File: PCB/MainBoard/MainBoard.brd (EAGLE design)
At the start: 60 x 75 mm, 94 parts, among them IC1 LD1085D2T33R, Q2 CSM-7X-DU, U1 LM1084IS-5.0/NOPB, U4 STM32H753VIT6, U5 LM1084IS-5.0/NOPB

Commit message: Update eagle files
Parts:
- removed C1, C4: 100nF, rcl:C0805
- removed C2, C3: 100uF, rcl:C0805
- removed U1: LM1084IS-5.0/NOPB, LM1084IS-5.0_NOPB:TO254P1524X483-4N
- moved ON/OFF 125.1 mm to (30.0, 22.0), turned to 180 degrees
- moved IC1 104.5 mm to (46.0, 36.0), flipped to the bottom, turned to 180 degrees
- moved C5 101.7 mm to (24.0, 37.0), flipped to the bottom, turned to 90 degrees
- moved PRAWY_TYL 92.7 mm to (14.0, 59.5)
- moved C32 92.0 mm to (128.6, 20.8)
- moved C21 92.0 mm to (117.5, 49.7)
- moved C43 91.0 mm to (115.3, 21.0)
- moved C33 91.0 mm to (116.6, 54.0)
- moved C19 91.0 mm to (133.3, 44.2)
- moved C22 91.0 mm to (111.7, 45.4)
- moved C23 91.0 mm to (111.6, 39.5)
- moved C35 91.0 mm to (135.7, 44.3)
- moved C36 91.0 mm to (109.0, 45.6)
- moved C40 91.0 mm to (127.8, 27.1)
- moved C41 91.0 mm to (115.7, 27.2)
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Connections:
- new net N$88: C24.2, C27.2, U5.1
- net +5V: now also C5.1, C6.1, IC1.3, U5.2, U5.4; no longer C3.1, C4.1, U1.2, U1.4
- net GND: no longer C1.2, C2.2, C24.2, C27.2, C3.2, C4.2, U1.1, U5.1
- net V_BAT: no longer C1.1, C2.1, C5.1, C6.1, IC1.3, U1.3, U5.2, U5.4
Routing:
- net +5V: track 0.00 -> 27.3 mm
- net V_BAT: track 0.00 -> 18.9 mm
- net +3V3: track 0.00 -> 5.57 mm
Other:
- outline, holes or cut-outs redrawn

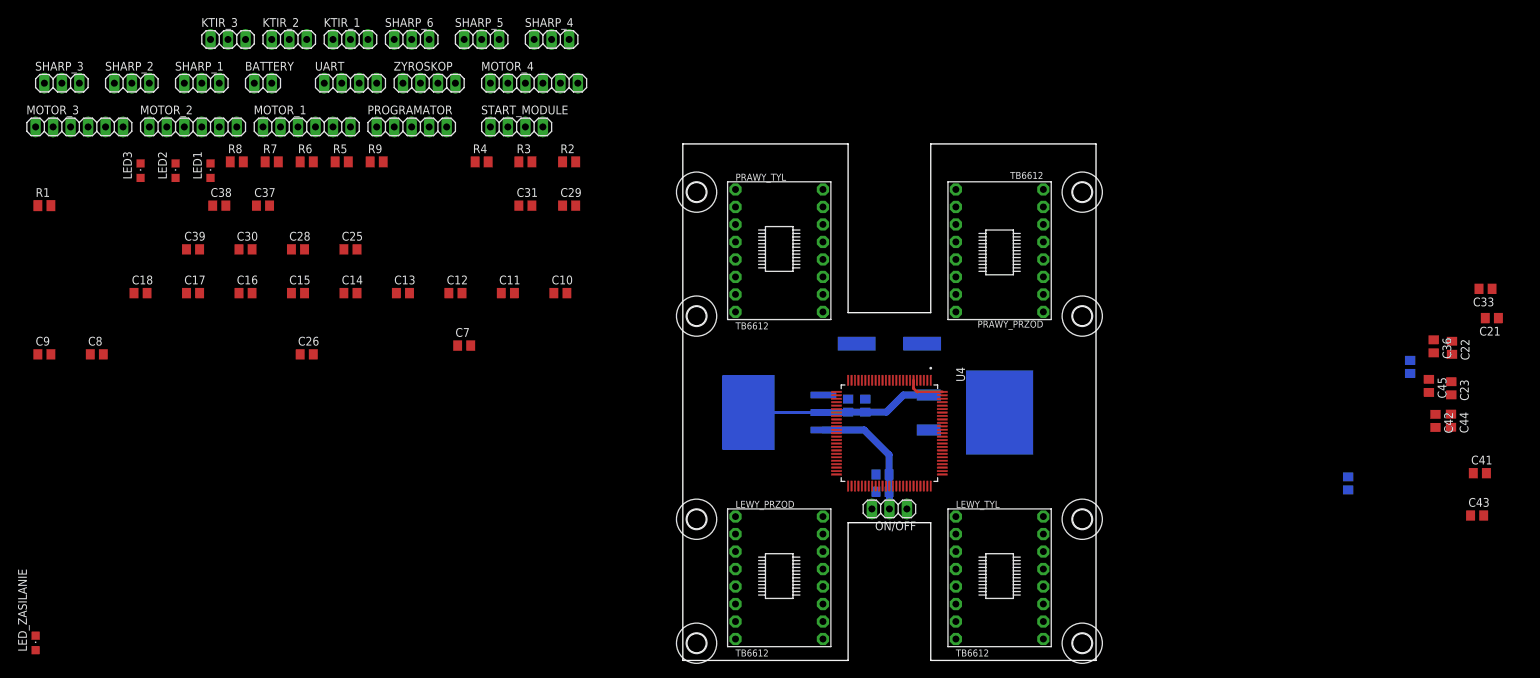
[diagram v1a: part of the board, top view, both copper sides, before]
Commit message: PCB update
-place elements on the board
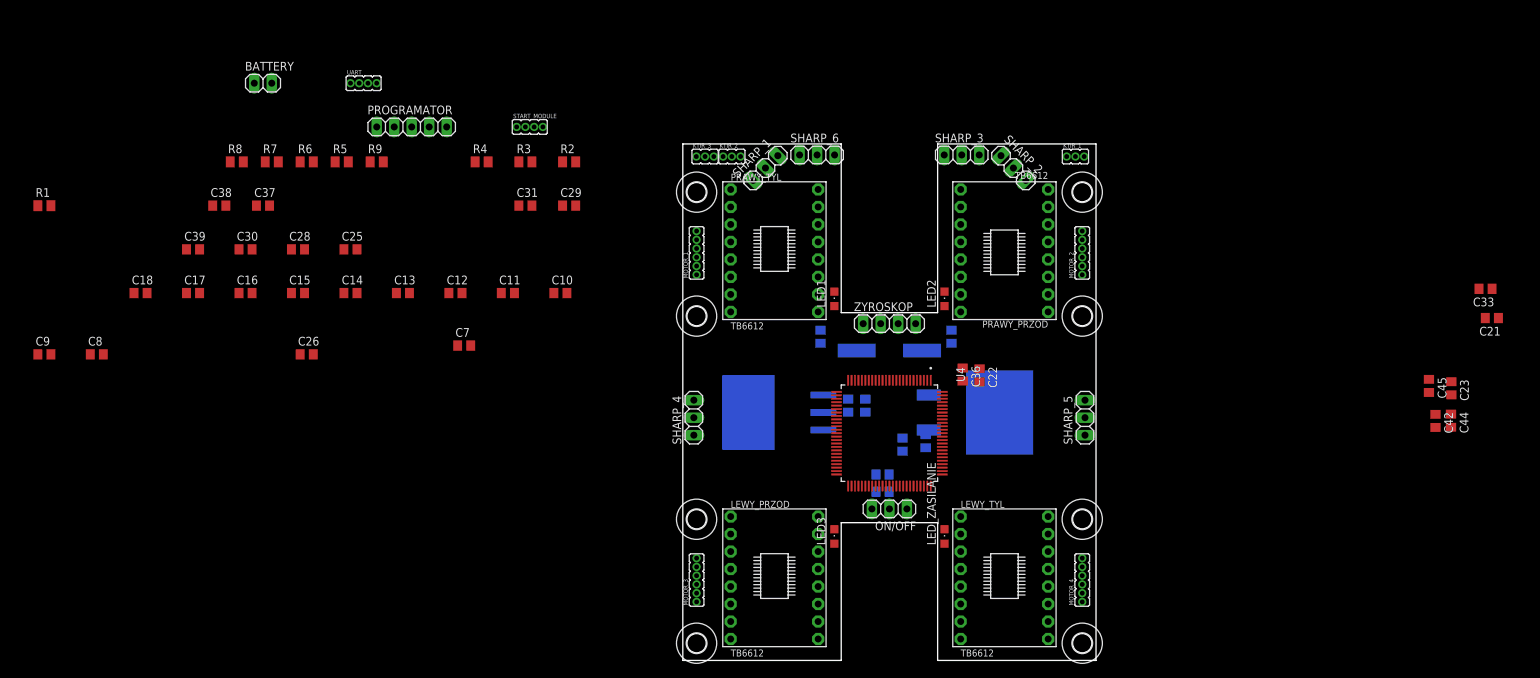
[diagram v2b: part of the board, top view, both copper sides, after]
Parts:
- KTIR_1, KTIR_2, KTIR_3: value (none) -> PH1X3-05; device pinhead:1X03 -> pinhrad:PH005-1-3
- MOTOR_1, MOTOR_2, MOTOR_3, MOTOR_4: value (none) -> PH1X6-05; device pinhead:1X06 -> pinhrad:PH005-1-6
- START_MODULE, UART: value (none) -> PH1X4-05; device pinhead:1X04 -> pinhrad:PH005-1-4
- moved LED_ZASILANIE 132.9 mm to (38.0, 18.0)
- moved SHARP_3 131.1 mm to (40.5, 73.4)
- moved MOTOR_2 130.9 mm to (58.0, 56.0), turned to 90 degrees
- moved SHARP_2 128.6 mm to (48.0, 71.5), turned to 315 degrees
- moved LED3 113.9 mm to (22.0, 18.0)
- moved LED2 113.2 mm to (38.0, 52.5)
- moved MOTOR_3 113.1 mm to (2.00, 8.50), turned to 90 degrees
- moved MOTOR_4 109.6 mm to (58.0, 8.50), turned to 90 degrees
- moved KTIR_1 105.4 mm to (55.7, 73.2)
- moved SHARP_5 103.4 mm to (58.4, 35.2), turned to 90 degrees
- moved LED1 92.5 mm to (22.0, 52.5)
- moved C41 83.9 mm to (31.9, 31.3), flipped to the bottom, turned to 270 degrees
- moved SHARP_1 82.8 mm to (12.0, 71.5), turned to 45 degrees
- moved C43 80.8 mm to (35.3, 31.8), flipped to the bottom, turned to 270 degrees
- moved C46 79.5 mm to (20.0, 47.0)
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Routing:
- net +5V: track 27.3 -> 0.00 mm
- net V_BAT: track 18.9 -> 0.00 mm
- net +3V3: track 5.57 -> 0.00 mm
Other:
- outline, holes or cut-outs redrawn

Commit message: Update pcb files
- edit positions on the board
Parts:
- added R13: 100R, rcl:M0805
- added R14, R15: 47R, rcl:M0805
- PROGRAMATOR: value (none) -> FTSH-107-01-F-DV-K; device pinhead:1X05 -> FTSH-107-01-F-DV-K:SAMTEC_FTSH-107-01-F-DV-K
- moved R8 118.8 mm to (38.1, 13.0), turned to 90 degrees
- moved BATTERY 113.5 mm to (34.0, 21.6)
- moved R7 100.9 mm to (21.9, 13.0), turned to 90 degrees
- moved START_MODULE 97.6 mm to (58.5, 25.5), turned to 90 degrees
- moved R6 93.9 mm to (38.1, 57.5), turned to 90 degrees
- moved UART 76.7 mm to (1.50, 25.5), turned to 90 degrees
- moved R5 73.0 mm to (21.9, 57.5), turned to 90 degrees
- moved PROGRAMATOR 65.9 mm to (11.0, 35.0), turned to 90 degrees
- moved ON/OFF 3.03 mm to (27.0, 21.6)
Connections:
- net N$30 renamed JRST
- removed net N$18: U4.60
- removed net N$22: U4.39
- removed net N$24: U4.28
- removed net N$25: U4.29
- removed net N$26: U4.30
- removed net N$27: U4.31
- removed net N$28: U4.77
- removed net N$29: U4.89
- removed net N$31: U4.91
- removed net N$33: U4.22
- removed net N$34: U4.23
- removed net N$38: U4.34
- removed net N$40: U4.93
- removed net N$43: U4.15
- removed net N$63: U4.43
- removed net N$65: U4.41
- removed net N$67: U4.61
- removed net N$74: U4.65
- removed net N$75: U4.64
- removed net N$76: U4.63
- removed net N$86: U4.72
- removed net N$87: U4.76
- removed net SWCLK: PROGRAMATOR.2
- removed net SWDIO: PROGRAMATOR.4
- new net JCLK: R15.1, U4.76
- new net JTDI: PROGRAMATOR.10, U4.77
- new net JTDO: PROGRAMATOR.08, U4.89
- new net JTMS: PROGRAMATOR.04, U4.72
- net +3V3: now also PROGRAMATOR.03; no longer PROGRAMATOR.1
- net BAT_ADC: now also U4.15
- net ENK_LP_A: now also U4.39
- net ENK_LP_B: now also U4.41
- net ENK_LT_B: now also U4.31, U4.91
- net ENK_PP_A: now also U4.59
- net ENK_PP_B: now also U4.60
- net ENK_PT_A: now also U4.63
- net ENK_PT_B: now also U4.64
- net GND: now also PROGRAMATOR.05, PROGRAMATOR.07, R13.2; no longer PROGRAMATOR.3
- net KTIR_1: now also U4.28
- net KTIR_2: now also U4.29
- net KTIR_3: now also U4.30
- net N$1: now also PROGRAMATOR.11, R13.1; no longer C25.2, R2.1, U4.14
- net N$17: now also PROGRAMATOR.06, R15.2; no longer U4.59
- net N$8: now also PROGRAMATOR.12, R14.2; no longer U4.92
- net NRST: now also C25.2, R14.1, R2.1, U4.14; no longer PROGRAMATOR.5
- net PWM_LP: now also U4.43
- net PWM_LT: now also U4.34
- net PWM_PP: now also U4.61
- net PWM_PT: now also U4.65
- net RX: now also U4.22
- net SCL: now also U4.92
- net SDA: now also U4.93
- net TX: now also U4.23

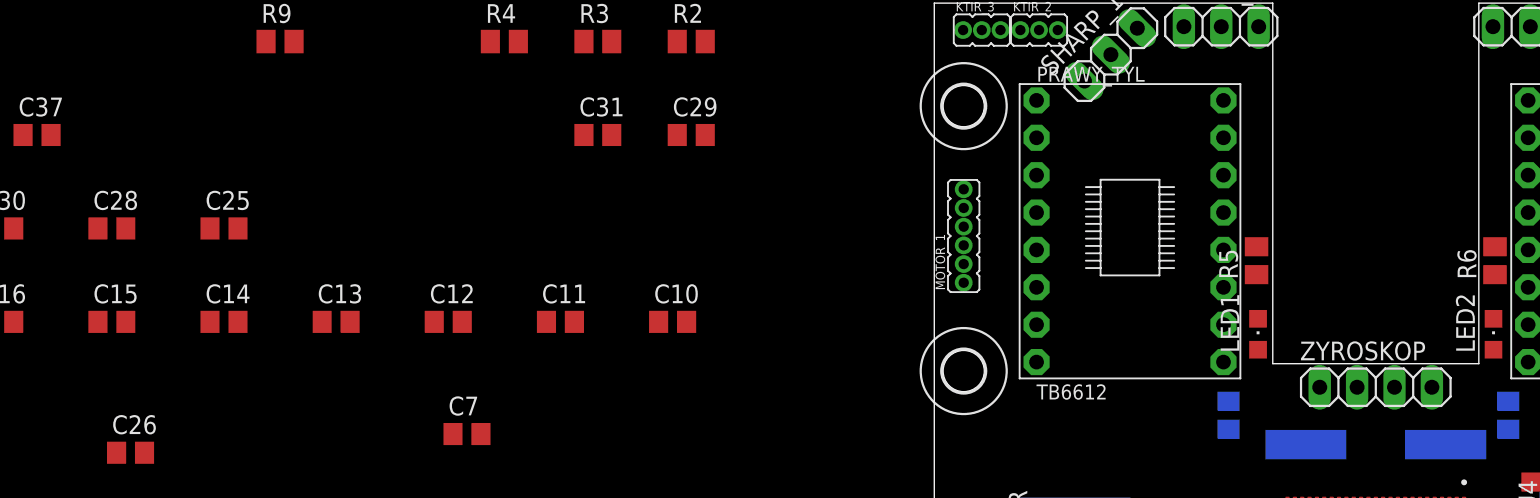
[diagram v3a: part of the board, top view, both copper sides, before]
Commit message: Update eagle files
-delete gyroscope
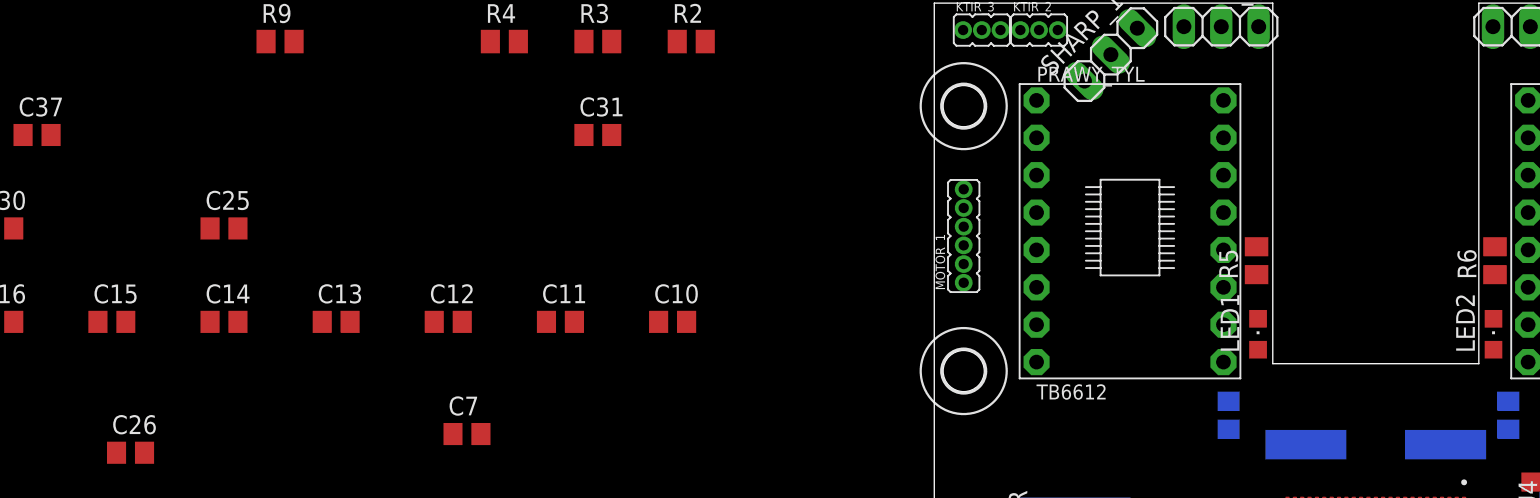
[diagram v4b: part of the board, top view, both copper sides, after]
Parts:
- removed C28: 100nF, rcl:C0805
- removed C29: 10uF, rcl:C0805
- removed ZYROSKOP: (no value), pinhead:1X04
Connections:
- net +3V3: no longer C28.2, C29.2, ZYROSKOP.4
- net GND: no longer C28.1, C29.1, ZYROSKOP.3
- net SCL: no longer ZYROSKOP.1
- net SDA: no longer ZYROSKOP.2
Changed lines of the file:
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@@
 <element name="C26" library="rcl" package="C0805" value="2.2uf(ceramic)" x="-54.61" y="44.45"/>
 <element name="C27" library="rcl" package="C0805" value="100uF" x="29" y="27" rot="MR0"/>
-<element name="C28" library="rcl" package="C0805" value="100nF" x="-55.88" y="59.69"/>
-<element name="C29" library="rcl" package="C0805" value="10uF" x="-16.51" y="66.04"/>
 <element name="C30" library="rcl" package="C0805" value="100nF" x="-63.5" y="59.69"/>
 <element name="C31" library="rcl" package="C0805" value="10uF" x="-22.86" y="66.04"/>
@@
 </element>
 <element name="UART" library="pinhrad" package="PH005-1-4" value="PH1X4-05" x="1.5" y="25.5" rot="R90"/>
-<element name="ZYROSKOP" library="pinhead" package="1X04" value="" x="30" y="48.9"/>
 <element name="U$1" library="holes" package="2,8" value="" x="2" y="2.5"/>
 <element name="U$2" library="holes" package="2,8" value="" x="2" y="20.5"/>
@@
 <contactref element="C37" pad="1"/>
 <contactref element="C18" pad="1"/>
-<contactref element="ZYROSKOP" pad="3"/>
-<contactref element="C29" pad="1"/>
-<contactref element="C28" pad="1"/>
 <contactref element="LED1" pad="C"/>
 <contactref element="LED2" pad="C"/>
@@
 <wire x1="24" y1="37.95" x2="26.5" y2="37.95" width="0" layer="19" extent="16-16"/>
 <wire x1="22.32" y1="39" x2="24" y2="37.95" width="0" layer="19" extent="1-16"/>
-<wire x1="31.27" y1="48.9" x2="39" y2="47.95" width="0" layer="19" extent="16-16"/>
 <wire x1="20" y1="47.95" x2="22.32" y2="39" width="0" layer="19" extent="1-16"/>
 <wire x1="19.65" y1="50.61" x2="20" y2="47.95" width="0" layer="19" extent="16-16"/>
 <wire x1="22" y1="53.55" x2="19.65" y2="50.61" width="0" layer="19" extent="1-1"/>
+<wire x1="13.035" y1="35" x2="22.32" y2="39" width="0" layer="19" extent="1-1"/>
+<wire x1="13.035" y1="33.73" x2="13.035" y2="35" width="0" layer="19" extent="1-1"/>
 <wire x1="22.32" y1="27.5" x2="24" y2="37.95" width="0" layer="19" extent="1-16"/>
 <wire x1="22" y1="19.05" x2="22.32" y2="27.5" width="0" layer="19" extent="1-1"/>
+<wire x1="1.6" y1="35.25" x2="13.035" y2="35" width="0" layer="19" extent="1-1"/>
+<wire x1="1.5" y1="28.04" x2="1.6" y2="35.25" width="0" layer="19" extent="1-1"/>
+<wire x1="6.95" y1="20.89" x2="1.5" y2="28.04" width="0" layer="19" extent="1-1"/>
+<wire x1="2" y1="14.85" x2="6.95" y2="20.89" width="0" layer="19" extent="1-1"/>
 <wire x1="6.95" y1="50.61" x2="19.65" y2="50.61" width="0" layer="19" extent="1-1"/>
 <wire x1="2" y1="62.35" x2="6.95" y2="50.61" width="0" layer="19" extent="1-1"/>
@@
 <wire x1="12" y1="71.5" x2="6.95" y2="68.39" width="0" layer="19" extent="1-1"/>
 <wire x1="19.5" y1="73.4" x2="12" y2="71.5" width="0" layer="19" extent="1-1"/>
+<wire x1="6.95" y1="3.11" x2="2" y2="14.85" width="0" layer="19" extent="1-1"/>
+<wire x1="19.65" y1="3.11" x2="6.95" y2="3.11" width="0" layer="19" extent="1-1"/>
 <wire x1="53.05" y1="50.61" x2="43.09" y2="42.35" width="0" layer="19" extent="1-1"/>
 <wire x1="58" y1="62.35" x2="53.05" y2="50.61" width="0" layer="19" extent="1-1"/>
@@
 <wire x1="40.5" y1="73.4" x2="48" y2="71.5" width="0" layer="19" extent="1-1"/>
 <wire x1="40.35" y1="68.39" x2="40.5" y2="73.4" width="0" layer="19" extent="1-1"/>
-<wire x1="6.95" y1="20.89" x2="22" y2="19.05" width="0" layer="19" extent="1-1"/>
-<wire x1="2" y1="14.85" x2="6.95" y2="20.89" width="0" layer="19" extent="1-1"/>
-<wire x1="1.5" y1="28.04" x2="6.95" y2="20.89" width="0" layer="19" extent="1-1"/>
-<wire x1="1.6" y1="35.25" x2="1.5" y2="28.04" width="0" layer="19" extent="1-1"/>
-<wire x1="6.95" y1="3.11" x2="2" y2="14.85" width="0" layer="19" extent="1-1"/>
-<wire x1="19.65" y1="3.11" x2="6.95" y2="3.11" width="0" layer="19" extent="1-1"/>
-<wire x1="-17.46" y1="66.04" x2="2" y2="62.35" width="0" layer="19" extent="1-1"/>
-<wire x1="-23.81" y1="66.04" x2="-17.46" y2="66.04" width="0" layer="19" extent="1-1"/>
-<wire x1="-30.16" y1="72.39" x2="-23.81" y2="66.04" width="0" layer="19" extent="1-1"/>
-<wire x1="-16.83" y1="53.34" x2="-17.46" y2="66.04" width="0" layer="19" extent="1-1"/>
+<wire x1="-16.83" y1="53.34" x2="2" y2="62.35" width="0" layer="19" extent="1-1"/>
 <wire x1="-24.45" y1="53.34" x2="-16.83" y2="53.34" width="0" layer="19" extent="1-1"/>
 <wire x1="-32.07" y1="53.34" x2="-24.45" y2="53.34" width="0" layer="19" extent="1-1"/>
@@
 <wire x1="-47.31" y1="53.34" x2="-39.69" y2="53.34" width="0" layer="19" extent="1-1"/>
 <wire x1="-49.21" y1="59.69" x2="-47.31" y2="53.34" width="0" layer="19" extent="1-1"/>
-<wire x1="-56.83" y1="59.69" x2="-49.21" y2="59.69" width="0" layer="19" extent="1-1"/>
-<wire x1="-56.83" y1="53.34" x2="-56.83" y2="59.69" width="0" layer="19" extent="1-1"/>
+<wire x1="-30.8" y1="45.72" x2="-32.07" y2="53.34" width="0" layer="19" extent="1-1"/>
+<wire x1="-56.83" y1="53.34" x2="-47.31" y2="53.34" width="0" layer="19" extent="1-1"/>
 <wire x1="-64.45" y1="53.34" x2="-56.83" y2="53.34" width="0" layer="19" extent="1-1"/>
 <wire x1="-64.45" y1="59.69" x2="-64.45" y2="53.34" width="0" layer="19" extent="1-1"/>
@@
 <wire x1="-61.91" y1="66.04" x2="-66.36" y2="66.04" width="0" layer="19" extent="1-1"/>
 <wire x1="-79.69" y1="53.34" x2="-72.07" y2="53.34" width="0" layer="19" extent="1-1"/>
-<wire x1="-30.8" y1="45.72" x2="-32.07" y2="53.34" width="0" layer="19" extent="1-1"/>
 <wire x1="-55.56" y1="44.45" x2="-56.83" y2="53.34" width="0" layer="19" extent="1-1"/>
 <wire x1="-84.14" y1="44.45" x2="-79.69" y2="53.34" width="0" layer="19" extent="1-1"/>
 <wire x1="-91.76" y1="44.45" x2="-84.14" y2="44.45" width="0" layer="19" extent="1-1"/>
+<wire x1="-23.81" y1="66.04" x2="-24.45" y2="53.34" width="0" layer="19" extent="1-1"/>
+<wire x1="-30.16" y1="72.39" x2="-23.81" y2="66.04" width="0" layer="19" extent="1-1"/>
 <wire x1="-93.66" y1="66.04" x2="-79.69" y2="53.34" width="0" layer="19" extent="1-1"/>
-<wire x1="13.035" y1="35" x2="-91.76" y2="44.45" width="0" layer="19" extent="1-1"/>
-<wire x1="13.035" y1="33.73" x2="13.035" y2="35" width="0" layer="19" extent="1-1"/>
-<wire x1="-112.05" y1="-26" x2="13.035" y2="33.73" width="0" layer="19" extent="1-1"/>
+<wire x1="-112.05" y1="-26" x2="-91.76" y2="44.45" width="0" layer="19" extent="1-1"/>
 </signal>
 <signal name="+3V3">
@@
 <contactref element="C17" pad="2"/>
 <contactref element="R2" pad="2"/>
-<contactref element="ZYROSKOP" pad="4"/>
-<contactref element="C28" pad="2"/>
-<contactref element="C29" pad="2"/>
 <contactref element="START_MODULE" pad="4"/>
 <contactref element="C31" pad="2"/>
@@
 <wire x1="26" y1="40.68" x2="31" y2="40.68" width="0" layer="19" extent="1-1"/>
 <wire x1="22.32" y1="38.5" x2="26" y2="40.68" width="0" layer="19" extent="1-1"/>
-<wire x1="33.81" y1="48.9" x2="33.5" y2="40.68" width="0" layer="19" extent="1-1"/>
 <wire x1="22.32" y1="27" x2="31.91" y2="30.39" width="0" layer="19" extent="1-16"/>
-<wire x1="40.35" y1="58.23" x2="33.81" y2="48.9" width="0" layer="19" extent="1-1"/>
-<wire x1="53.05" y1="53.15" x2="40.35" y2="58.23" width="0" layer="19" extent="1-1"/>
-<wire x1="58" y1="58.54" x2="53.05" y2="53.15" width="0" layer="19" extent="1-1"/>
+<wire x1="13.035" y1="32.46" x2="22.32" y2="27" width="0" layer="19" extent="1-1"/>
 <wire x1="19.65" y1="13.27" x2="22.32" y2="27" width="0" layer="19" extent="1-1"/>
 <wire x1="6.95" y1="18.35" x2="19.65" y2="13.27" width="0" layer="19" extent="1-1"/>
 <wire x1="2" y1="11.04" x2="6.95" y2="18.35" width="0" layer="19" extent="1-1"/>
+<wire x1="53.05" y1="53.15" x2="43.09" y2="40.45" width="0" layer="19" extent="1-1"/>
+<wire x1="58" y1="58.54" x2="53.05" y2="53.15" width="0" layer="19" extent="1-1"/>
+<wire x1="40.35" y1="58.23" x2="53.05" y2="53.15" width="0" layer="19" extent="1-1"/>
 <wire x1="57.01" y1="73.17" x2="58" y2="58.54" width="0" layer="19" extent="1-1"/>
-<wire x1="19.65" y1="60.77" x2="33.81" y2="48.9" width="0" layer="19" extent="1-1"/>
+<wire x1="19.65" y1="60.77" x2="40.35" y2="58.23" width="0" layer="19" extent="1-1"/>
 <wire x1="6.95" y1="65.85" x2="19.65" y2="60.77" width="0" layer="19" extent="1-1"/>
 <wire x1="7.12" y1="73.17" x2="6.95" y2="65.85" width="0" layer="19" extent="1-1"/>
@@
 <wire x1="2" y1="58.54" x2="6.95" y2="65.85" width="0" layer="19" extent="1-1"/>
 <wire x1="-15.56" y1="72.39" x2="3.23" y2="73.17" width="0" layer="19" extent="1-1"/>
-<wire x1="-15.56" y1="66.04" x2="-15.56" y2="72.39" width="0" layer="19" extent="1-1"/>
-<wire x1="-21.91" y1="66.04" x2="-15.56" y2="66.04" width="0" layer="19" extent="1-1"/>
-<wire x1="-54.93" y1="59.69" x2="-21.91" y2="66.04" width="0" layer="19" extent="1-1"/>
-<wire x1="-54.93" y1="53.34" x2="-54.93" y2="59.69" width="0" layer="19" extent="1-1"/>
+<wire x1="-21.91" y1="66.04" x2="-15.56" y2="72.39" width="0" layer="19" extent="1-1"/>
+<wire x1="-54.93" y1="53.34" x2="-21.91" y2="66.04" width="0" layer="19" extent="1-1"/>
 <wire x1="-62.55" y1="53.34" x2="-54.93" y2="53.34" width="0" layer="19" extent="1-1"/>
 <wire x1="-62.55" y1="59.69" x2="-62.55" y2="53.34" width="0" layer="19" extent="1-1"/>
 <wire x1="-70.17" y1="53.34" x2="-62.55" y2="53.34" width="0" layer="19" extent="1-1"/>
-<wire x1="13.035" y1="32.46" x2="-70.17" y2="53.34" width="0" layer="19" extent="1-1"/>
 </signal>
 <signal name="MOT_LP2">
@@
 </signal>
 <signal name="SCL">
-<contactref element="ZYROSKOP" pad="1"/>
 <contactref element="U4" pad="92"/>
-<wire x1="37.68" y1="35" x2="26.19" y2="48.9" width="0" layer="19" extent="1-1"/>
 </signal>
 <signal name="SDA">
-<contactref element="ZYROSKOP" pad="2"/>
 <contactref element="U4" pad="93"/>
-<wire x1="37.68" y1="35.5" x2="28.73" y2="48.9" width="0" layer="19" extent="1-1"/>
 </signal>
 <signal name="TX">
